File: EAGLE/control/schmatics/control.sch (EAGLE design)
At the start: 0 parts

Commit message: end of night commit
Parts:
- added C1, C2, C3, C4, C5, C6: (no value), rcl:C-US025-024X044
- added IC1, IC2, IC3: 74LS14N, 74xx-us:74LS14N
- added IC4: 74LS109N, 74xx-us:74LS109N
- added R1, R10, R11, R12, R2, R3, R4, R5, R6, R7, R8, R9: (no value), rcl:R-US_0204/7
- added S1, S2, S4, S5: (no value), switch-omron:10-XX
- added S3: (no value), switch:255SB
- added U1: CD4052BE, cd family:CD4052BE
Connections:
- new net +5V: IC4A.J, IC4A.PRE, R1.2, R11.2, R3.2, R5.2, R8.2, R9.2, U1.VDD
- new net BRIGHT: IC3A.O
- new net GND: C1.2, C2.2, C3.2, C4.2, C5.2, C6.2, IC4A.K, S1.P, S1.P1, S2.P, S2.P1, S3.P, S4.P, S4.P1, S5.P, S5.P1, U1.INH, U1.VEE, U1.VSS
- new net HALT: IC4A.Q, U1.A
- new net HLT_TG: IC2A.O, IC4A.CLK
- new net HR_PB: IC1B.O
- new net INC_LG: IC1D.O
- new net INC_SM: IC1C.O
- new net INIT_NEG: IC4A.CLR
- new net MIN_PB: IC1A.O
- new net N$1: R1.1, R2.2, S1.S, S1.S1
- new net N$11: C5.1, IC2A.I, R10.1
- new net N$12: R11.1, R12.2, S5.S, S5.S1
- new net N$13: C6.1, IC3A.I, R12.1
- new net N$2: C1.1, IC1A.I, R2.1
- new net N$3: R3.1, R4.2, S2.S, S2.S1
- new net N$4: C2.1, IC1B.I, R4.1
- new net N$5: R5.1, R7.2, S3.O
- new net N$6: C4.1, IC1C.I, R7.1
- new net N$7: R6.2, R8.1, S3.S
- new net N$8: C3.1, IC1D.I, R6.1
- new net N$9: R10.2, R9.1, S4.S, S4.S1

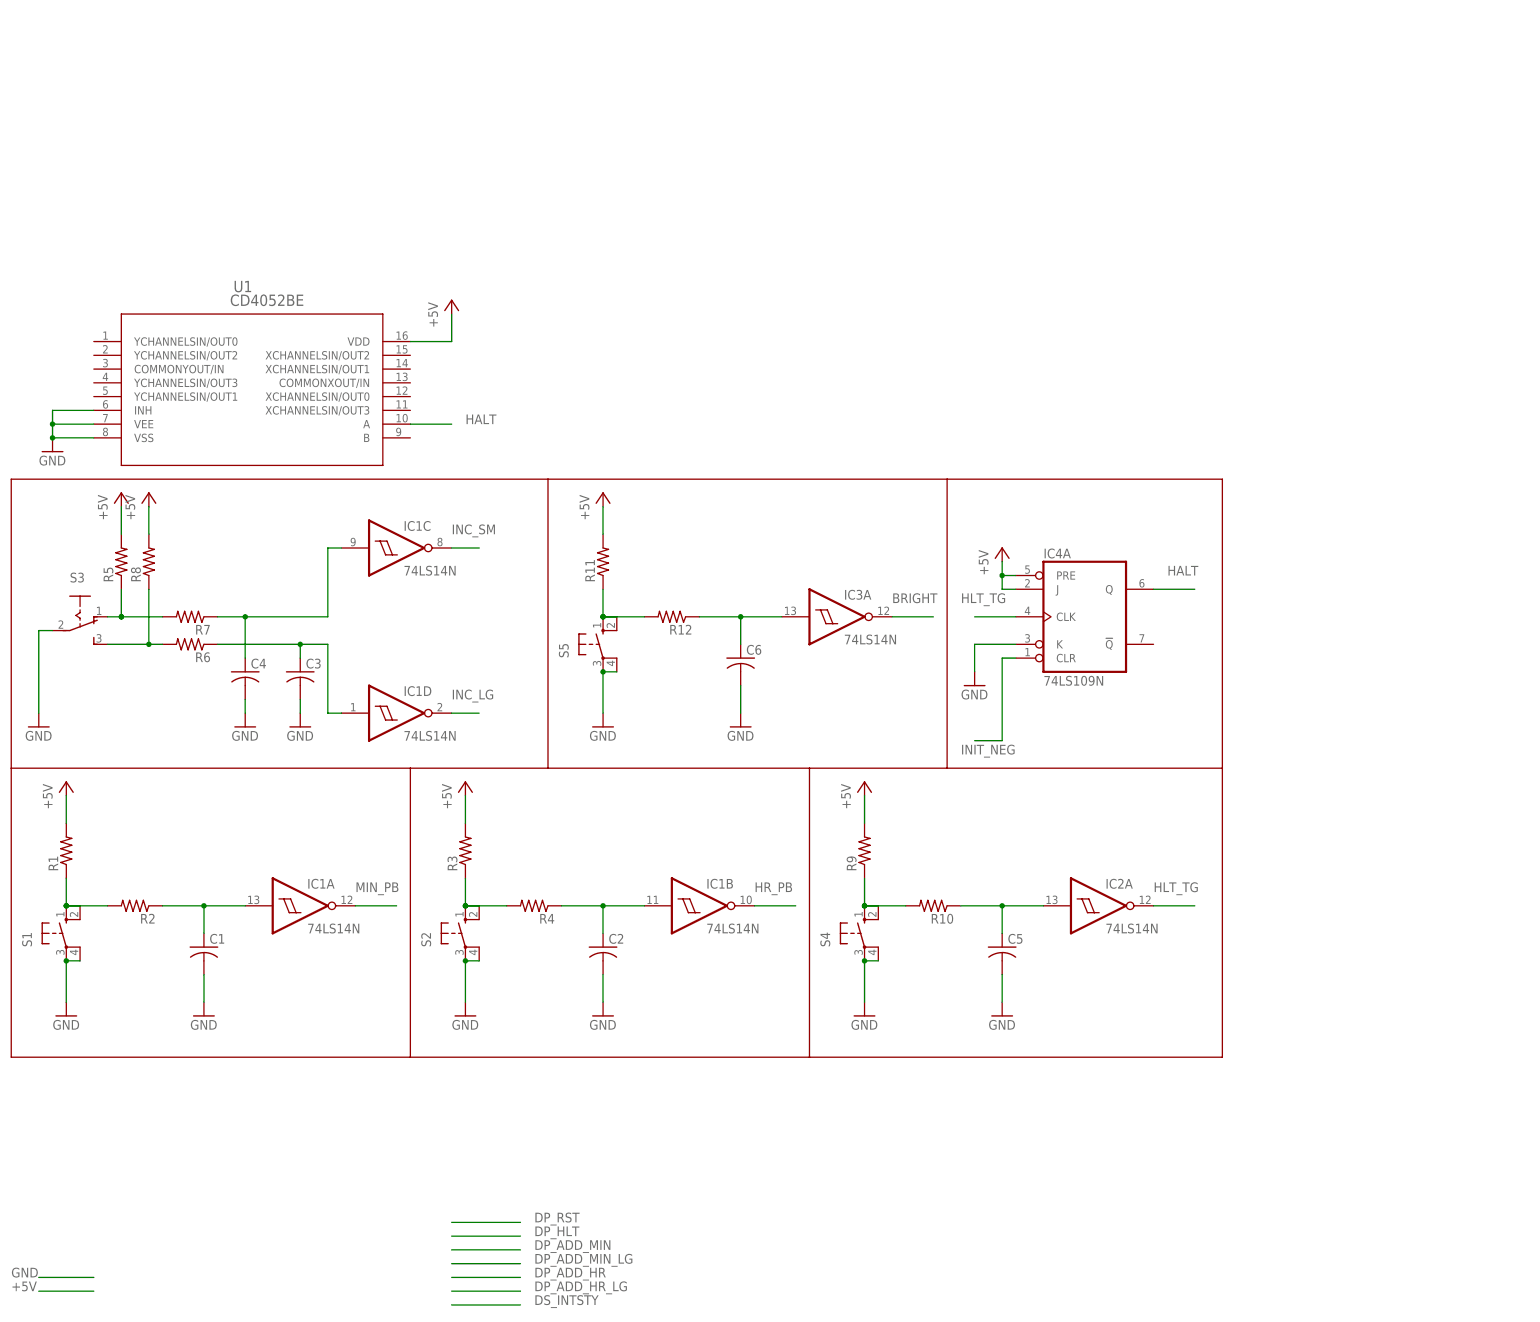
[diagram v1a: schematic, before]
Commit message: Finished CD4052b and DP_RST/HLT
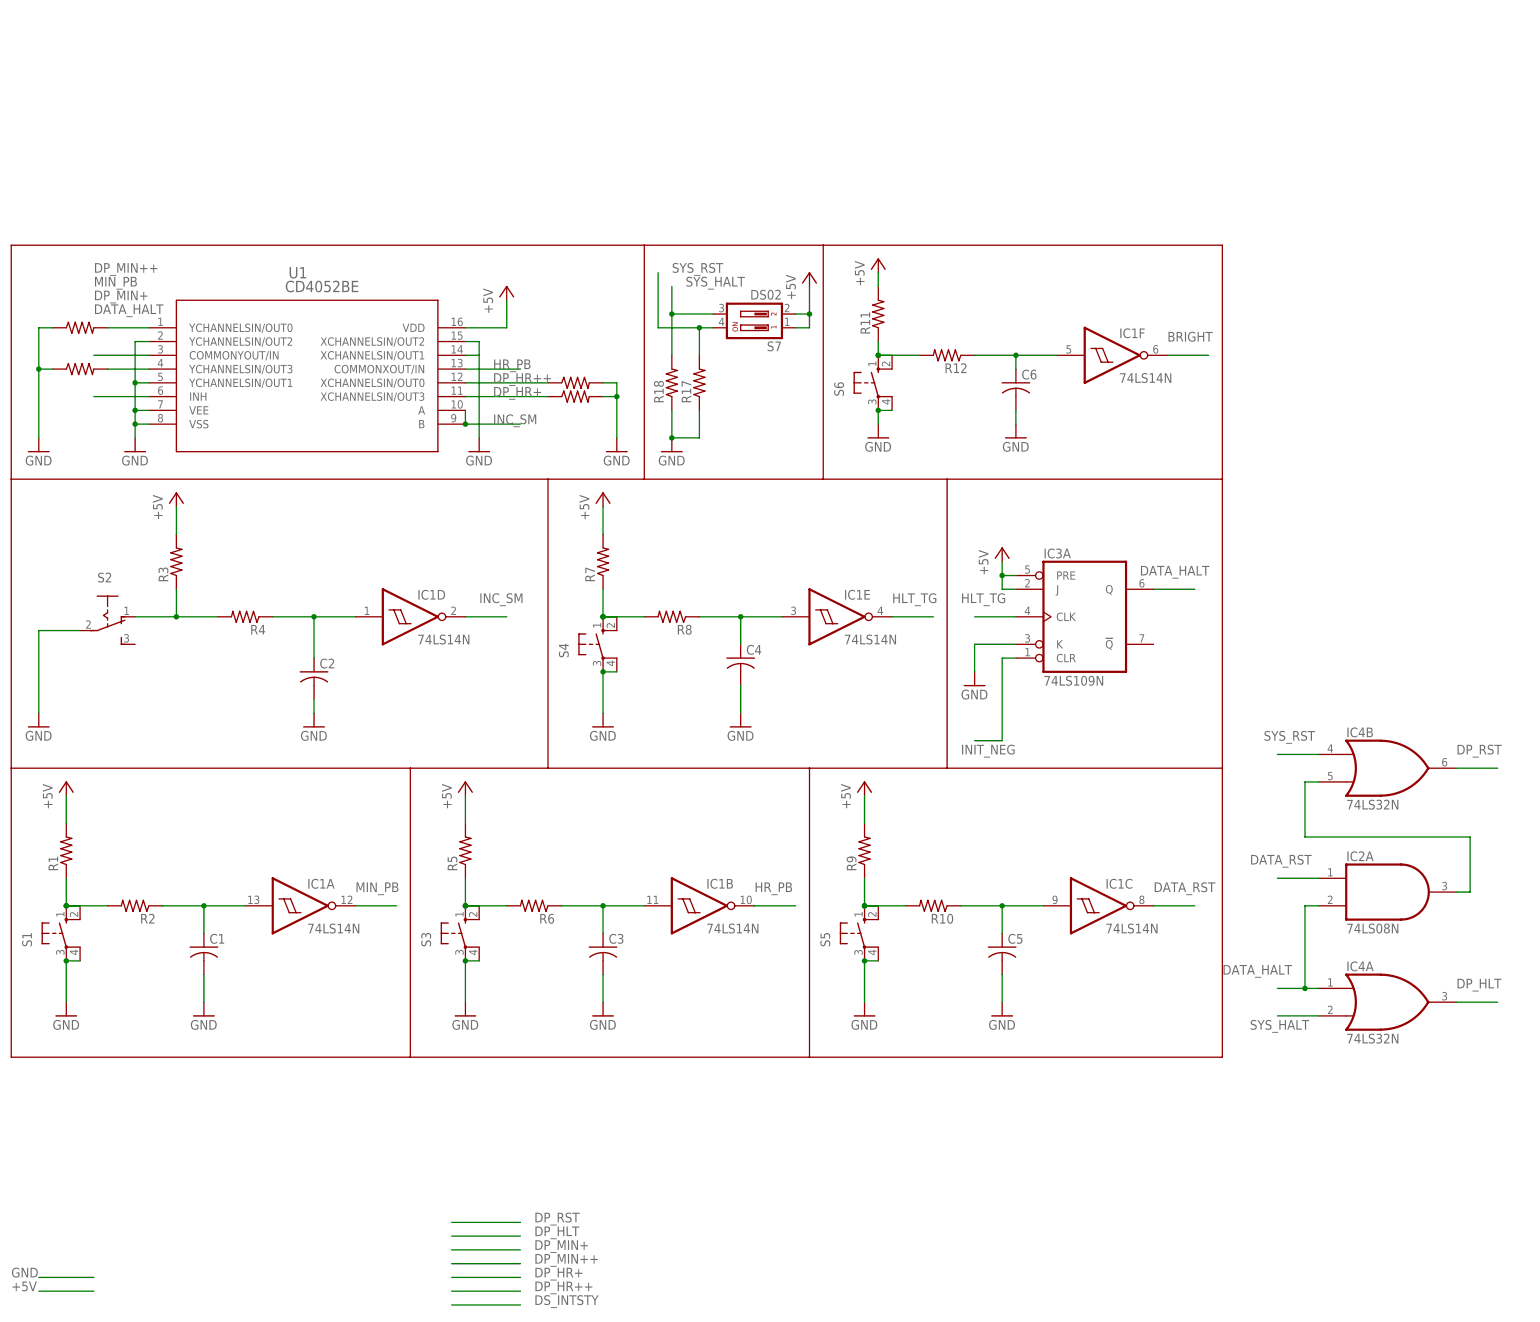
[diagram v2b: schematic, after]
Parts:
- added R13, R14, R15, R16, R17, R18: (no value), rcl:R-US_0204/7
- added S6: (no value), switch-omron:10-XX
- added S7: DS02, Switch:DS02
- IC2: value 74LS14N -> 74LS08N; device 74xx-us:74LS14N -> 74xx-us:74LS08N
- IC3: value 74LS14N -> 74LS109N; device 74xx-us:74LS14N -> 74xx-us:74LS109N
- IC4: value 74LS109N -> 74LS32N; device 74xx-us:74LS109N -> 74xx-us:74LS32N
- S2: device switch-omron:10-XX -> switch:255SB
- S3: device switch:255SB -> switch-omron:10-XX
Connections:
- removed net HALT: IC4A.Q, U1.A
- removed net INC_LG: IC1D.O
- new net DATA_HALT: IC2A.I1, IC3A.Q, IC4A.I0, U1.INH
- new net DATA_RST: IC1C.O, IC2A.I0
- new net DP_HLT: IC4A.O
- new net DP_HR+: R16.1, U1.XCHANNELSIN/OUT3
- new net DP_HR++: R15.1, U1.XCHANNELSIN/OUT0
- new net DP_MIN+: R14.2, U1.YCHANNELSIN/OUT3
- new net DP_MIN++: R13.2, U1.YCHANNELSIN/OUT0
- new net DP_RST: IC4B.O
- new net N$10: IC2A.O, IC4B.I1
- new net N$16: U1.XCHANNELSIN/OUT1
- new net SYS_HALT: IC4A.I1, R18.2, S7.3
- new net SYS_RST: IC4B.I0, R17.2, S7.4
- net +5V: now also IC3A.J, IC3A.PRE, R7.2, S7.1, S7.2; no longer IC4A.J, IC4A.PRE, R8.2
- net BRIGHT: now also IC1F.O; no longer IC3A.O
- net GND: now also IC3A.K, R13.1, R14.1, R15.2, R16.2, R17.1, R18.1, S3.P1, S6.P, S6.P1, U1.XCHANNELSIN/OUT2, U1.YCHANNELSIN/OUT1, U1.YCHANNELSIN/OUT2; no longer IC4A.K, S2.P1, U1.INH
- net HLT_TG: now also IC1E.O, IC3A.CLK; no longer IC2A.O, IC4A.CLK
- net HR_PB: now also U1.COMMONXOUT/IN
- net INC_SM: now also IC1D.O, U1.A, U1.B; no longer IC1C.O
- net INIT_NEG: now also IC3A.CLR; no longer IC4A.CLR
- net MIN_PB: now also U1.COMMONYOUT/IN
- net N$11: now also IC1C.I; no longer IC2A.I
- net N$12: now also R7.1, R8.2, S4.S, S4.S1; no longer R11.1, R12.2, S5.S, S5.S1
- net N$13: now also C4.1, IC1E.I, R8.1; no longer C6.1, IC3A.I, R12.1
- net N$3: now also R5.1, R6.2, S3.S, S3.S1; no longer R3.1, R4.2, S2.S, S2.S1
- net N$4: now also C3.1, R6.1; no longer C2.1, R4.1
- net N$5: now also R3.1, R4.2, S2.O; no longer R5.1, R7.2, S3.O
- net N$6: now also C2.1, IC1D.I, R4.1; no longer C4.1, IC1C.I, R7.1
- net N$7: now also R11.1, R12.2, S6.S, S6.S1; no longer R6.2, R8.1, S3.S
- net N$8: now also C6.1, IC1F.I, R12.1; no longer C3.1, IC1D.I, R6.1
- net N$9: now also S5.S, S5.S1; no longer S4.S, S4.S1
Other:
- moved on the sheet: C2, C3, C4, C6, IC1C, IC1D, R11, R12, R3, R4, R5, R6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

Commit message: Finished Control Circuit Skeleton
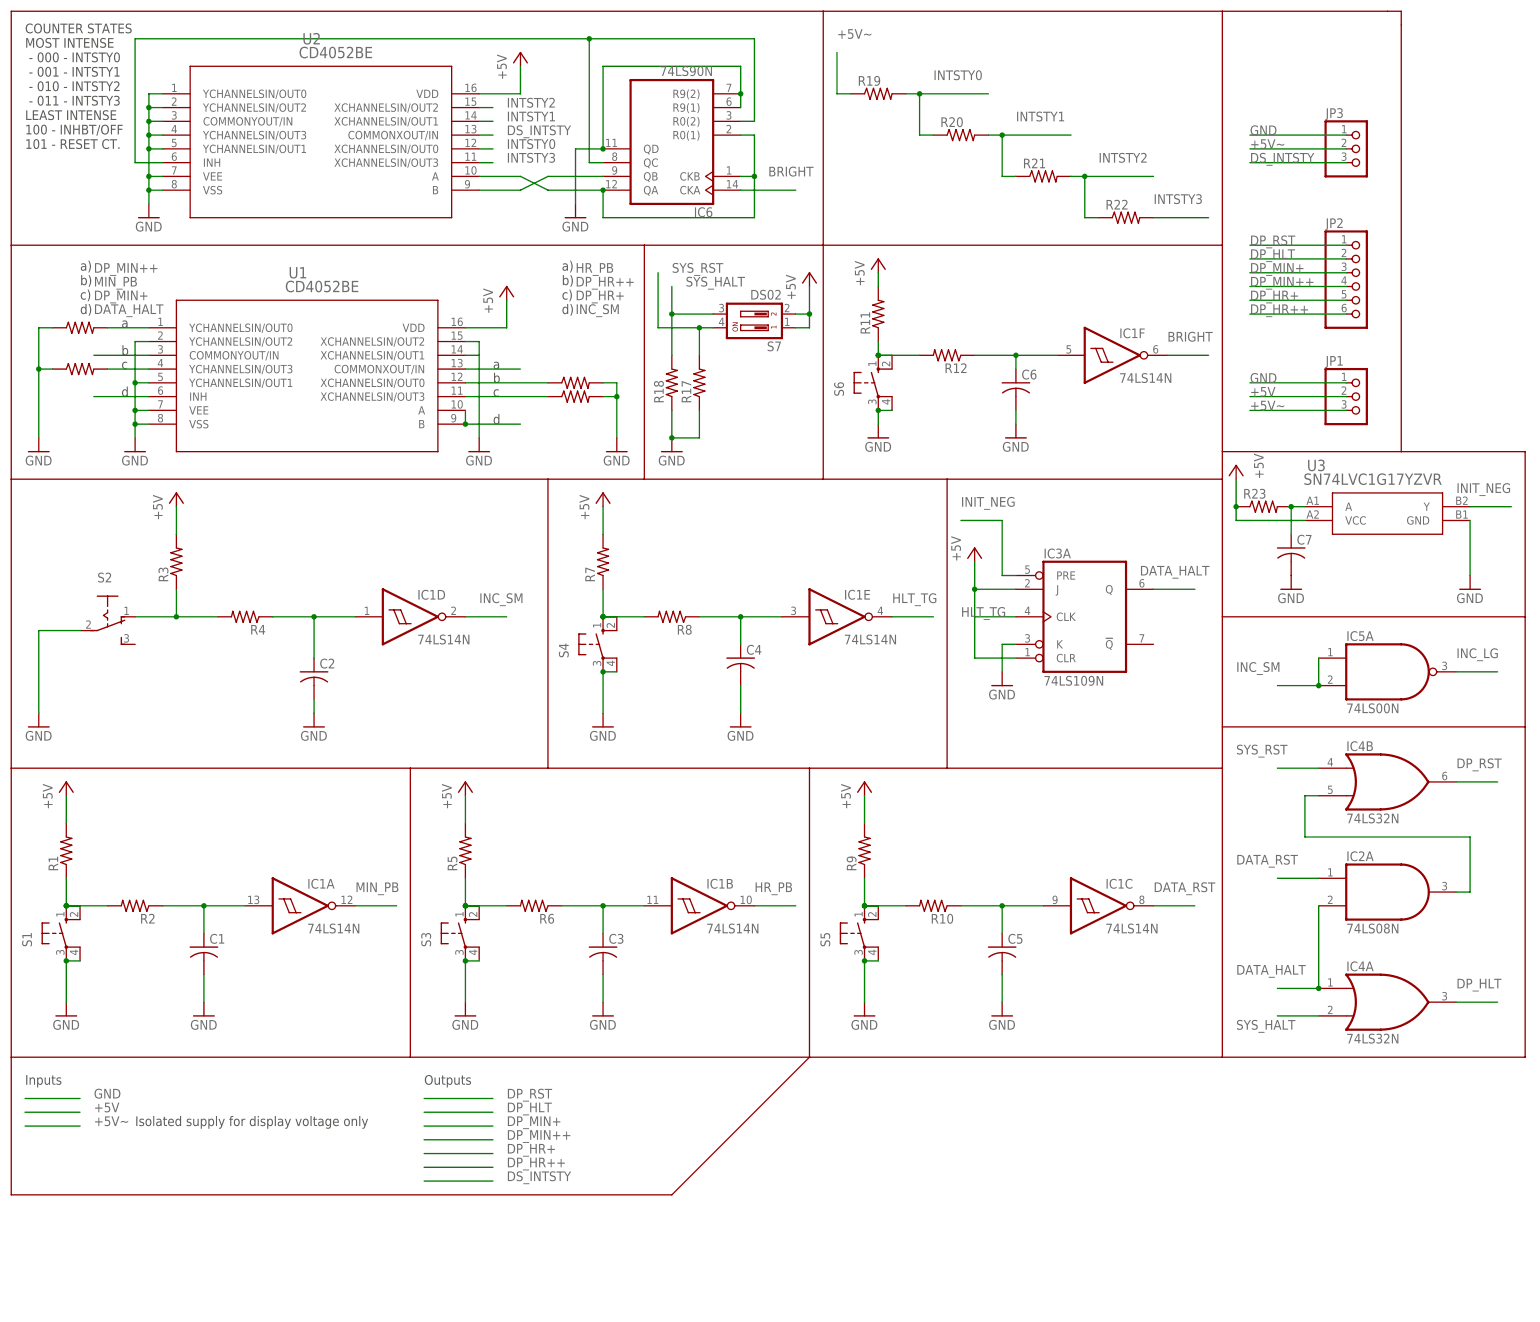
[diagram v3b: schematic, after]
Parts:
- added C7: (no value), rcl:C-US025-025X050
- added IC5: 74LS00N, 74xx-us:74LS00N
- added IC6: 74LS90N, 74xx-us:74LS90N
- added JP1, JP3: (no value), pinhead:PINHD-1X3
- added JP2: (no value), pinhead:PINHD-1X6
- added R19, R20, R21, R22, R23: (no value), rcl:R-US_0204/7
- added U2: CD4052BE, cd family:CD4052BE
- added U3: SN74LVC1G17YZVR, SN74LVC1G17YZVR:SN74LVC1G17YZVR
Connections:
- new net +5V~: JP1.3, JP3.2, R19.1
- new net DS_INTSTY: JP3.3, U2.COMMONXOUT/IN
- new net INC_LG: IC5A.O
- new net INTSTY0: R19.2, R20.1, U2.XCHANNELSIN/OUT0
- new net INTSTY1: R20.2, R21.1, U2.XCHANNELSIN/OUT1
- new net INTSTY2: R21.2, R22.1, U2.XCHANNELSIN/OUT2
- new net INTSTY3: R22.2, U2.XCHANNELSIN/OUT3
- new net N$14: IC6A.QC, IC6A.R0(2), U2.INH
- new net N$15: C7.1, R23.2, U3.A
- new net N$17: IC6A.QB, U2.B
- new net N$18: IC6A.CKB, IC6A.QA, IC6A.R0(1), U2.A
- net +5V: now also IC3A.CLR, JP1.2, R23.1, U2.VDD, U3.VCC; no longer IC3A.PRE
- net BRIGHT: now also IC6A.CKA
- net DP_HLT: now also JP2.2
- net DP_HR+: now also JP2.5
- net DP_HR++: now also JP2.6
- net DP_MIN+: now also JP2.3
- net DP_MIN++: now also JP2.4
- net DP_RST: now also JP2.1
- net GND: now also C7.2, IC6A.QD, IC6A.R9(1), IC6A.R9(2), JP1.1, JP3.1, U2.COMMONYOUT/IN, U2.VEE, U2.VSS, U2.YCHANNELSIN/OUT0, U2.YCHANNELSIN/OUT1, U2.YCHANNELSIN/OUT2, U2.YCHANNELSIN/OUT3, U3.GND
- net INC_SM: now also IC5A.I0, IC5A.I1
- net INIT_NEG: now also IC3A.PRE, U3.Y; no longer IC3A.CLR
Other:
- note added: "COUNTER STATES MOST INTENSE - 000 - INTSTY0 - 001 - INTSTY1 - 010 - INTSTY2 - 011 - INTSTY3 LEAST INTENSE 100 - INHBT/OFF 101 - RESET CT."
- note added: "Inputs"
- note added: "Isolated supply for display voltage only"
- note added: "Outputs"
- note added: "a"
- note added: "a) b) c) d)"
- note added: "b"
- note added: "c"
- note added: "d"
- moved on the sheet: IC4B
